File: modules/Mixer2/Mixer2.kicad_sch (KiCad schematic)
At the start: 40 parts, among them U1 TL074, U2 TL074, U3 TL072

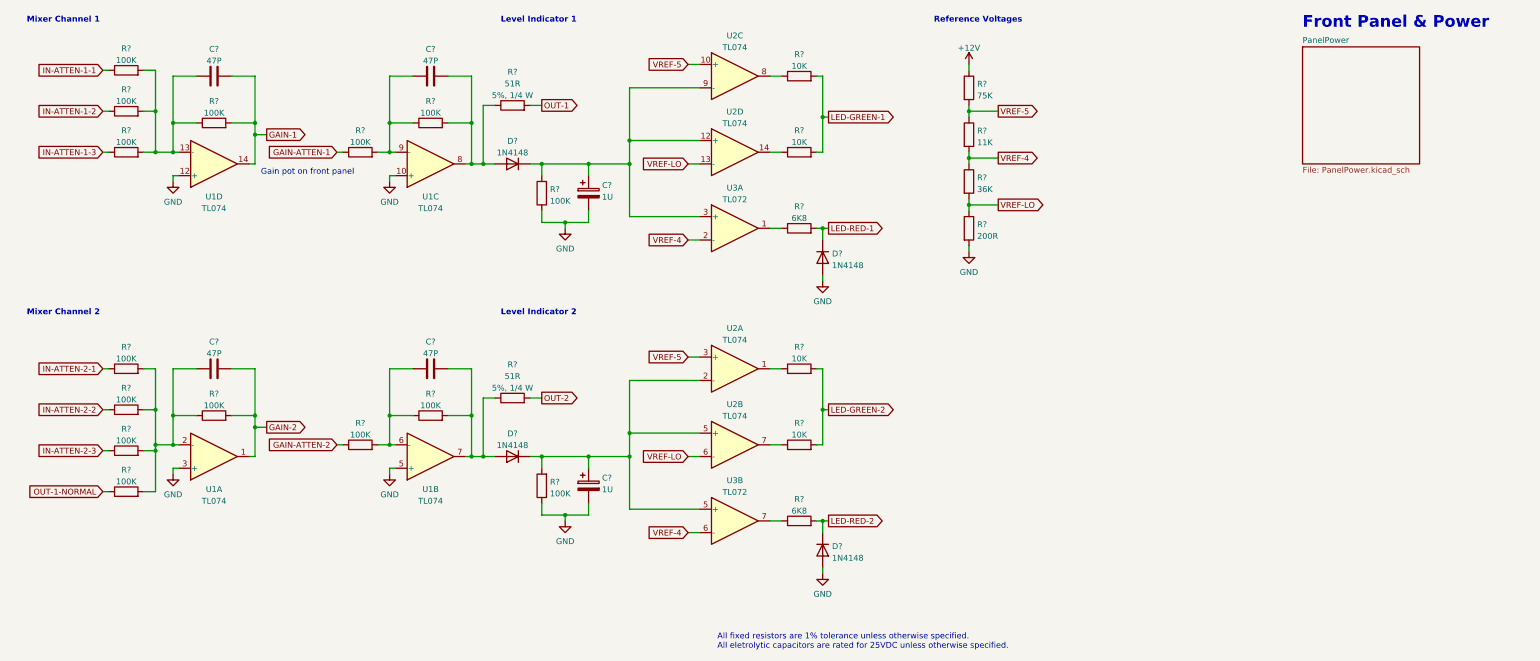
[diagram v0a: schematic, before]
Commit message: Mixer2 - annotate the schematic
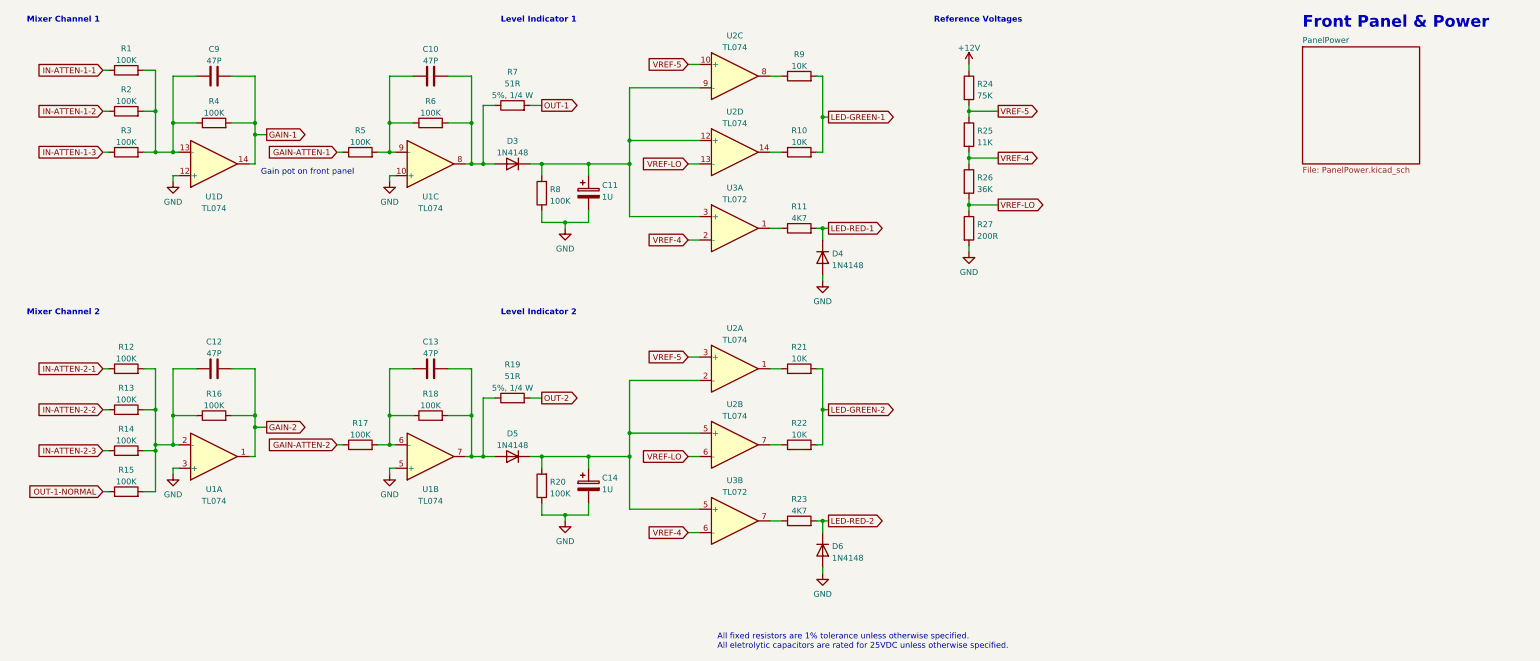
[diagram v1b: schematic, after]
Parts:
- R11, R23: renamed from R?; value 6K8 -> 4K7
- gave numbers to parts that had none: 35

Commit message: Mixer2 - footprints & BOM
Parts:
- removed C11, C14: 1U, symbol -lmp:CP
- added C11, C14: 100N, -lmp-misc:C_Disc_D5.0mm_W2.5mm_P2.50mm, symbol -lmp:CC_100N
- C10, C12, C13, C9: footprint (none) -> -lmp-misc:C_Disc_D5.0mm_W2.5mm_P2.50mm; Distributor (none) -> Mouser; DistributorPartLink (none) -> https://www.mouser.ca/ProductDetail/Vishay-BC-Components/K4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; DistributorPartNum (none) -> 594-K470K15C0GH53L2; Manufacturer (none) -> Vishay; ManufacturerPartNum (none) -> K470K15C0GH53L2
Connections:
- net GND: now also C11.2, C14.2
- net at D5.1 (K), R20.2, U2.2 (-)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: now also C14.1
- net at D3.1 (K), R8.2, U2.12 (+)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: now also C11.1

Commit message: Mixer2 - wip
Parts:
- added D4, D7: 1N4148, Diode_THT:D_DO-35_SOD27_P7.62mm_Horizontal, symbol -lmp-diode:1N4148
- renumbered D4 to D5, D5 to D6, D6 to D8
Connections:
- net GAIN-ATTEN-1: now also D4.2 (A)
- net GAIN-ATTEN-2: now also D7.2 (A)
- net at C14.1, D6.1 (K), R20.2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: now also D7.1 (K)
- net at C11.1, D3.1 (K), R8.2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: now also D4.1 (K)
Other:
- moved on the sheet: C10, C11, C13, C14, D5, D8, R10, R11, R17, R18, R19, R20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

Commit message: Mixer2 - BOM wip
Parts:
- R1, R12, R13, R14, R15, R16, R17, R18, R2, R20, R3, R4, R5, R6, R8: DistributorPartLink https://www.mouser.ca/c/?m=YAGEO&power+rating=166+mW+(1%2f6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 -> https://www.mouser.ca/ProductDetail/YAGEO/MFR-12FTF52-100K?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; DistributorPartNum 603-MFR-12* -> 603-MFR-12FTF52-100K; ManufacturerPartNum MFR-12* -> MFR-12FTF52-100K
- R10, R21, R22, R9: DistributorPartLink https://www.mouser.ca/c/?m=YAGEO&power+rating=166+mW+(1%2f6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 -> https://www.mouser.ca/ProductDetail/YAGEO/MFR-12FTF52-10K?q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; DistributorPartNum 603-MFR-12* -> 603-MFR-12FTF52-10K; ManufacturerPartNum MFR-12* -> MFR-12FTF52-10K
- R11, R23: DistributorPartLink https://www.mouser.ca/c/?m=YAGEO&power+rating=166+mW+(1%2f6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 -> https://www.mouser.ca/ProductDetail/YAGEO/MFR-12FTF52-4K7?q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; DistributorPartNum 603-MFR-12* -> 603-MFR-12FTF52-4K7; ManufacturerPartNum MFR-12* -> MFR-12FTF52-4K7
- R24: DistributorPartLink https://www.mouser.ca/c/?m=YAGEO&power+rating=166+mW+(1%2f6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 -> https://www.mouser.ca/ProductDetail/YAGEO/MFR-12FTF52-75K?q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; DistributorPartNum 603-MFR-12* -> 603-MFR-12FTF52-75K; ManufacturerPartNum MFR-12* -> MFR-12FTF52-75K
- R25: DistributorPartLink https://www.mouser.ca/c/?m=YAGEO&power+rating=166+mW+(1%2f6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 -> https://www.mouser.ca/ProductDetail/YAGEO/MFR-12FTF52-11K?q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; DistributorPartNum 603-MFR-12* -> 603-MFR-12FTF52-11K; ManufacturerPartNum MFR-12* -> MFR-12FTF52-11K
- R26: DistributorPartLink https://www.mouser.ca/c/?m=YAGEO&power+rating=166+mW+(1%2f6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 -> https://www.mouser.ca/ProductDetail/YAGEO/MFR-12FTF52-36K?q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; DistributorPartNum 603-MFR-12* -> 603-MFR-12FTF52-36K; ManufacturerPartNum MFR-12* -> MFR-12FTF52-36K
- R27: DistributorPartLink https://www.mouser.ca/c/?m=YAGEO&power+rating=166+mW+(1%2f6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 -> https://www.mouser.ca/ProductDetail/603-MFR-12FTF52-200R; DistributorPartNum 603-MFR-12* -> 603-MFR-12FTF52-200R; ManufacturerPartNum MFR-12* -> MFR-12FTF52-200R

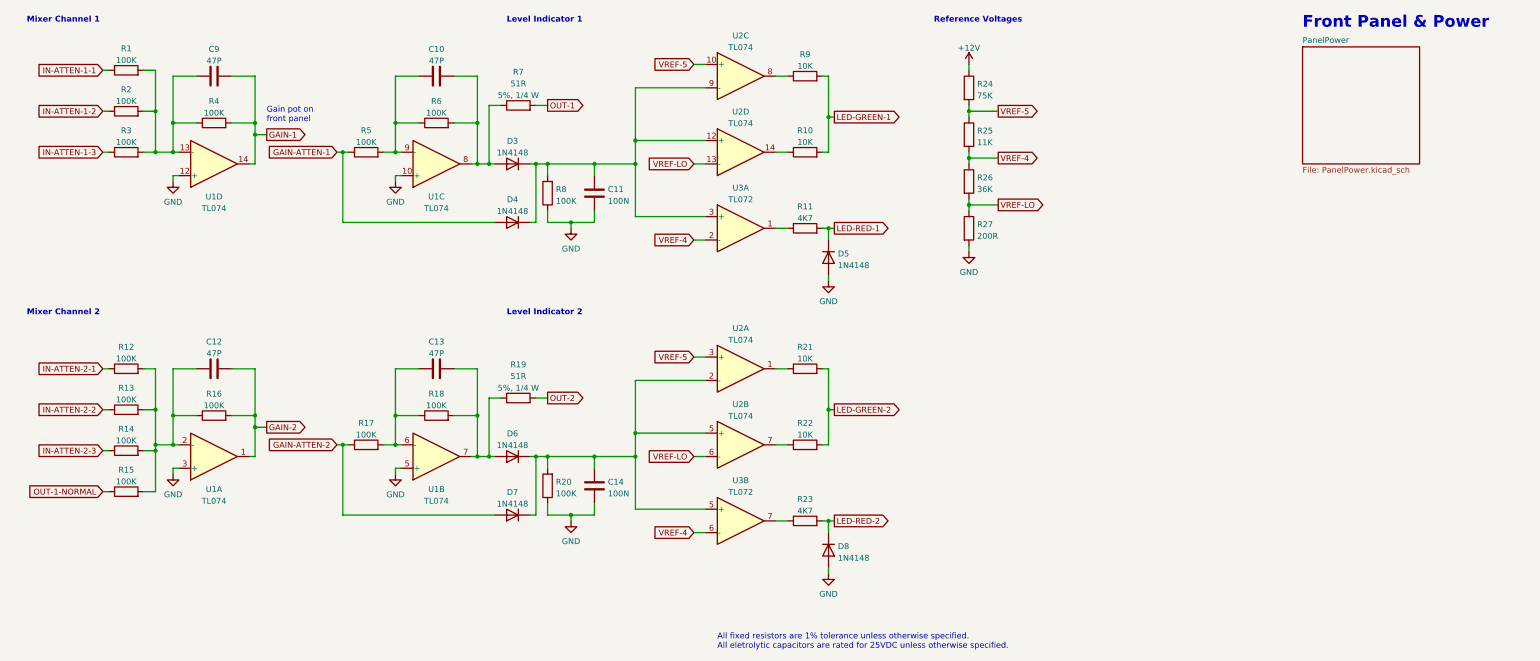
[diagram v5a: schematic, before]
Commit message: Mixer2 - remove bad diodes
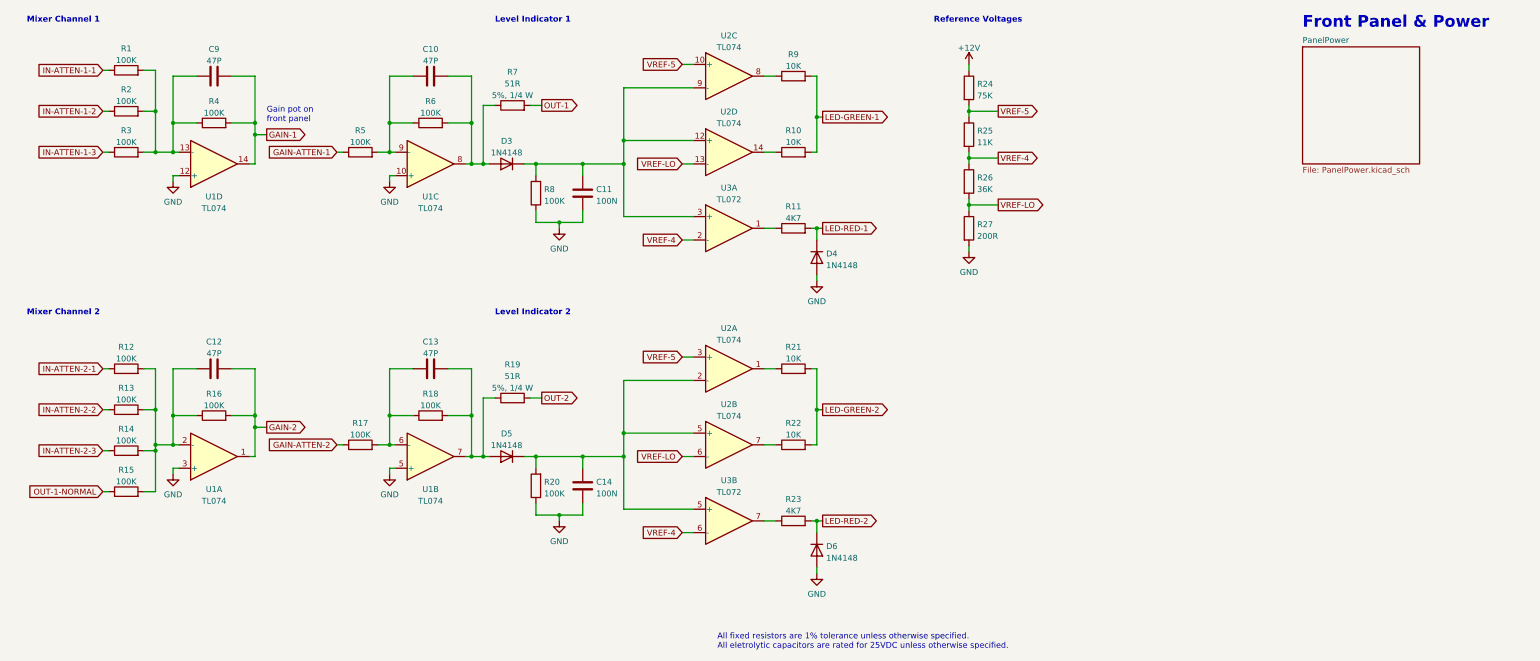
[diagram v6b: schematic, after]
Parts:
- removed D4, D7: 1N4148, Diode_THT:D_DO-35_SOD27_P7.62mm_Horizontal, symbol -lmp-diode:1N4148
- renumbered D5 to D4, D6 to D5, D8 to D6
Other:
- moved on the sheet: C10, C11, C13, C14, D3, D4, D5, D6, R10, R11, R17, R18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

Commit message: Mixer2: fix level indicators - wip
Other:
- note added: "Mixer 1"
- note added: "Mixer 2"
- note added: "TODO: connect level indicator before gain control? Requires reversing level indicator voltages."
- note removed: "Mixer Channel 1"
- note removed: "Mixer Channel 2"
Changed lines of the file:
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@@
+    (effects (font (size 1.27 1.27)) (justify left bottom))
+  )
+  (text "TODO: connect level indicator before gain control?\nRequires reversing level indicator voltages."
+    (at 85.09 66.04 0)
     (effects (font (size 1.27 1.27)) (justify left bottom))
   )
@@
     (effects (font (size 1.27 1.27) (thickness 0.254) bold) (justify left bottom))
   )
-  (text "Mixer Channel 1" (at 27.94 20.32 0)
+  (text "Mixer 1" (at 27.94 20.32 0)
     (effects (font (size 1.27 1.27) (thickness 0.254) bold) (justify left bottom))
   )
-  (text "Mixer Channel 2" (at 27.94 83.82 0)
+  (text "Mixer 2" (at 27.94 83.82 0)
     (effects (font (size 1.27 1.27) (thickness 0.254) bold) (justify left bottom))
   )

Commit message: Mixer2: fix level indicators - wip
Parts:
- D3, D5: value 1N4148 -> 1N5711; symbol -lmp-diode:1N4148 -> -lmp-diode:1N5711; DistributorPartLink https://www.mouser.ca/ProductDetail/?qs=0lQeLiL1qyZS6rosZp7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 -> https://www.mouser.ca/ProductDetail/STMicroelectronics/1N57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; DistributorPartNum 512-1N4148T50R -> 511-1N5711; Manufacturer On Semi / Fairchild -> STMicroelectronics; ManufacturerPartNum 1N4148-T50R -> 1N5711
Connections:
- net GAIN-1: now also D3.1 (K)
- net GAIN-2: now also D5.1 (K)
- net at C14.1, R20.2, U2.2 (-)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: now also D5.2 (A); no longer D5.1 (K)
- net at C10.2, R6.2, R7.1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: no longer D3.2 (A)
- net at C11.1, R8.2, U2.12 (+)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: now also D3.2 (A); no longer D3.1 (K)
- net at C13.2, R18.2, R19.1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: no longer D5.2 (A)
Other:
- note removed: "TODO: connect level indicator before gain control? Requires reversing level indicator voltages."
- moved on the sheet: C11, C12, C13, C14, D3, D4, D5, D6, R10, R11, R12, R13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
